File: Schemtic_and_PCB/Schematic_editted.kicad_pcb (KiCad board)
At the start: 2 copper layers, 124.5 x 120.7 mm, 187 parts, among them J1 Light_Sensor, J11 Conn_01x02_Pin, J12 Boot0, J13 USB_B_Micro, J14 VSOURCE_3.3V_Boot, J15 VSOURCE_3.3V_Boot, J16 SWD Debugger, J17 Conn_01x02_Pin, J18 Conn_01x22_Pin, J19 Conn_01x22_Pin, J2 Conn_01x04_Pin, J20 PB12-PB15, J21 PA15 - PB5, J22 PB6 -PB9, J23 VBAT -PC13 -GND -3.3, J24 PA0 - PA1 -PA2 -GND, J25 PA3 -PA6, J26 PB3 -PB6, J27 PB3 -PB6, J28 PA3 -PA6, J29 BOOT1, J3 Conn_01x03_Pin, J30 GND, J31 GND, J32 Conn_01x01_Pin, J33 Conn_01x04_Pin, J34 Conn_01x04_Socket, J37 Jack-DC, J39 Conn_01x02_Pin, J4 Conn_01x22_Socket, J5 Conn_01x22_Socket, J6 Conn_01x04_Pin, J7 COnnector_Light, J8 Conn_01x04_Pin, J9 Conn_01x04_Pin, K1 SANYOU_SRD_Form_C, K2 SANYOU_SRD_Form_C, K3 SANYOU_SRD_Form_C, Q1 NPN, Q2 NPN, Q3 NPN, Q4 MMBT3906, Q5 MMBT3906, Q6 IRF7343PBF, SW1 SW_Push, U1 AMS1117-3.3, U10 ICL7662CBA-T, U11 AMS1117-3.3, U2 LM393, U3 CA3140, U4 STM32F103C8Tx, U5 TL081, U6 CA3140, U7 TL081, U8 LM2596S-ADJ, U9 DHT11, Y1 8MHz, Y2 32.768K

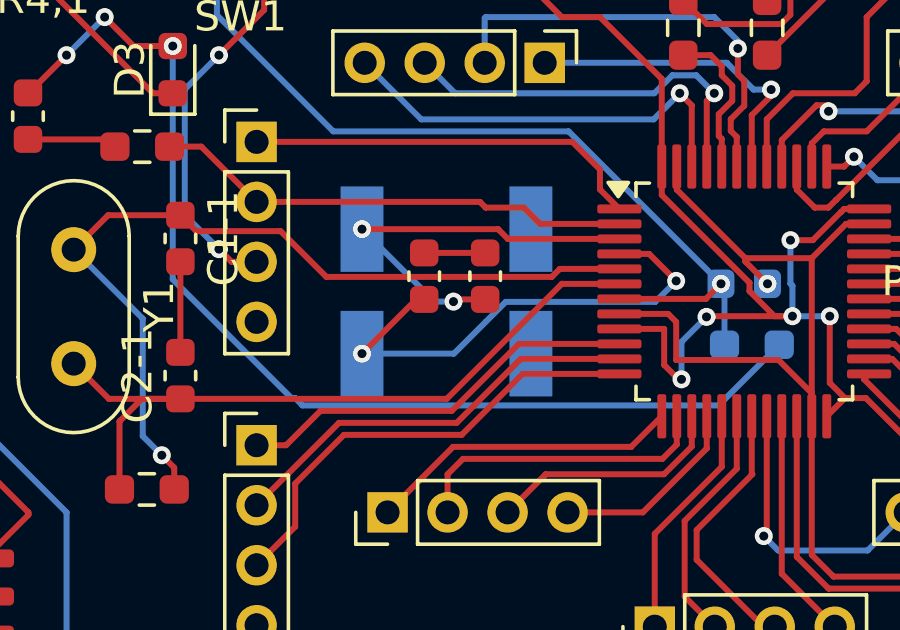
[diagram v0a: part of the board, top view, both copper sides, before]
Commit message: ADd stm32
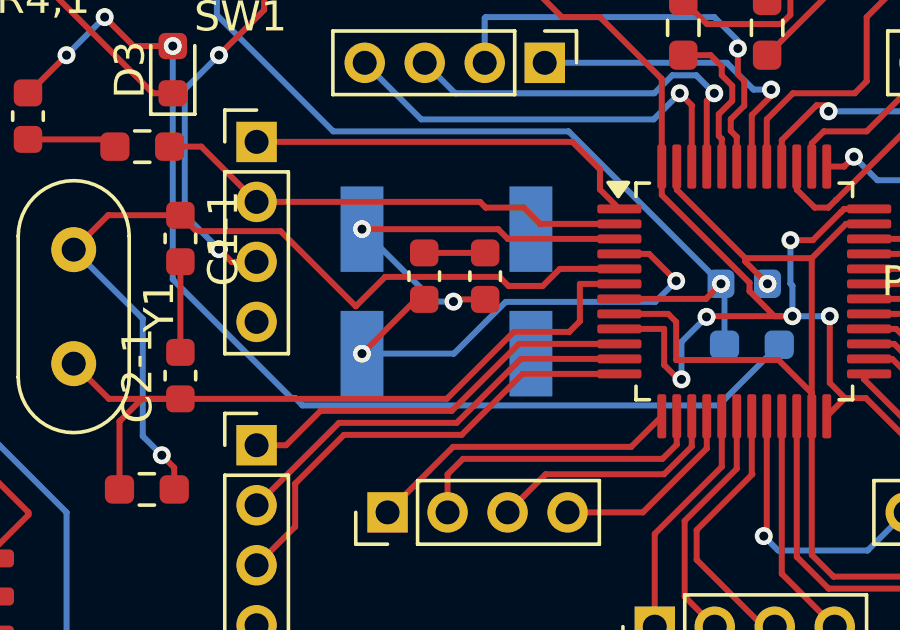
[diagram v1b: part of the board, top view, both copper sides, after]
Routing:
- net OSC_IN: track 29.0 -> 30.1 mm
- net OSC_OUT: track 24.9 -> 25.6 mm
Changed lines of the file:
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@@
 	)
 	(segment
-		(start 140.215 93.495)
-		(end 143.025 93.495)
+		(start 150.317696 95.021)
+		(end 150.619 95.322304)
 		(width 0.2)
 		(layer "F.Cu")
@@
 	)
 	(segment
-		(start 144.551 95.021)
-		(end 152.063314 95.021)
+		(start 150.619 95.322304)
+		(end 151.76201 95.322304)
 		(width 0.2)
 		(layer "F.Cu")
@@
 	)
 	(segment
+		(start 143.025 93.495)
+		(end 145.53 96)
+		(width 0.2)
+		(layer "F.Cu")
+		(net 5)
+	)
+	(segment
+		(start 145.53 96)
+		(end 146.509 95.021)
+		(width 0.2)
+		(layer "F.Cu")
+		(net 5)
+	)
+	(segment
 		(start 139.065 100.965)
 		(end 139.479 101.379)
@@
 	)
 	(segment
-		(start 152.330314 94.754)
-		(end 154.3175 94.754)
-		(width 0.2)
-		(layer "F.Cu")
-		(net 5)
-	)
-	(segment
-		(start 152.063314 95.021)
+		(start 151.76201 95.322304)
 		(end 152.330314 94.754)
 		(width 0.2)
@@
 	)
 	(segment
-		(start 143.025 93.495)
-		(end 144.551 95.021)
+		(start 146.509 95.021)
+		(end 150.317696 95.021)
+		(width 0.2)
+		(layer "F.Cu")
+		(net 5)
+	)
+	(segment
+		(start 140.215 93.495)
+		(end 143.025 93.495)
+		(width 0.2)
+		(layer "F.Cu")
+		(net 5)
+	)
+	(segment
+		(start 152.330314 94.754)
+		(end 154.3175 94.754)
 		(width 0.2)
 		(layer "F.Cu")
@@
 	)
 	(segment
-		(start 148.564 99.086)
-		(end 152.4 95.25)
-		(width 0.2)
-		(layer "F.Cu")
-		(net 7)
-	)
-	(segment
-		(start 152.404 95.254)
-		(end 154.3175 95.254)
-		(width 0.2)
-		(layer "F.Cu")
-		(net 7)
-	)
-	(segment
-		(start 139.684 99.086)
-		(end 148.564 99.086)
-		(width 0.2)
-		(layer "F.Cu")
-		(net 7)
-	)
-	(segment
 		(start 137.654 99.836)
 		(end 137.654 102.104)
@@
 	)
 	(segment
-		(start 152.4 95.25)
-		(end 152.404 95.254)
+		(start 150.796 96.854)
+		(end 152.646 96.854)
 		(width 0.2)
 		(layer "F.Cu")
@@
 		(start 138.404 99.086)
 		(end 137.654 99.836)
+		(width 0.2)
+		(layer "F.Cu")
+		(net 7)
+	)
+	(segment
+		(start 152.646 96.854)
+		(end 153 96.5)
+		(width 0.2)
+		(layer "F.Cu")
+		(net 7)
+	)
+	(segment
+		(start 153 95.254)
+		(end 154.3175 95.254)
 		(width 0.2)
 		(layer "F.Cu")
@@
 		(width 0.2)
 		(layer "F.Cu")
+		(net 7)
+	)
+	(segment
+		(start 139.684 99.086)
+		(end 148.564 99.086)
+		(width 0.2)
+		(layer "F.Cu")
+		(net 7)
+	)
+	(segment
+		(start 148.564 99.086)
+		(end 150.796 96.854)
+		(width 0.2)
+		(layer "F.Cu")
+		(net 7)
+	)
+	(segment
+		(start 153 96.5)
+		(end 153 95.254)
+		(width 0.2)
+		(layer "F.Cu")
